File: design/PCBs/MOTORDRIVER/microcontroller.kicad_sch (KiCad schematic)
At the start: 14 parts, among them IC1 ATSAME53J18A-MF

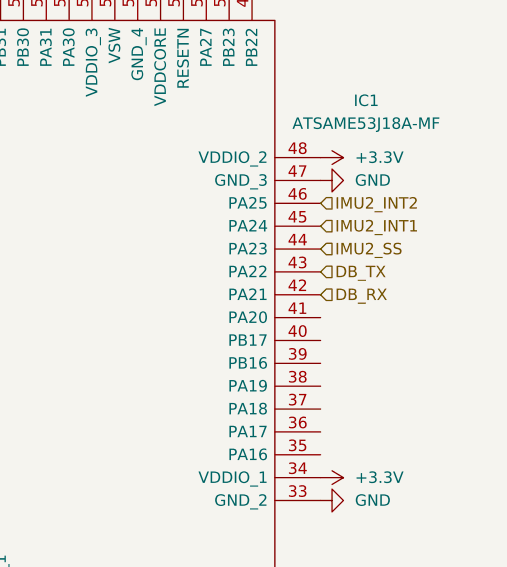
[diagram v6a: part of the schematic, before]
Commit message: added power ic
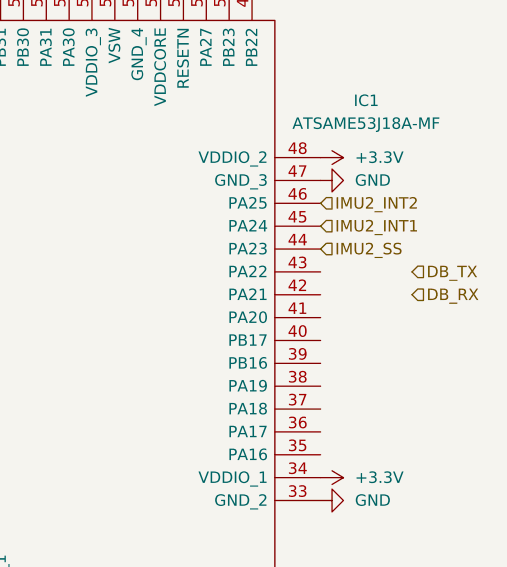
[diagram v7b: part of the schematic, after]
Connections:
- net DB_RX: no longer IC1.42 (PA21)
- net DB_TX: no longer IC1.43 (PA22)
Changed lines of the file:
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@@
 	(hierarchical_label "DB_RX"
 		(shape input)
-		(at 173.99 105.41 0)
+		(at 184.15 105.41 0)
 		(fields_autoplaced yes)
 		(effects
@@
 	(hierarchical_label "DB_TX"
 		(shape input)
-		(at 173.99 102.87 0)
+		(at 184.15 102.87 0)
 		(fields_autoplaced yes)
 		(effects

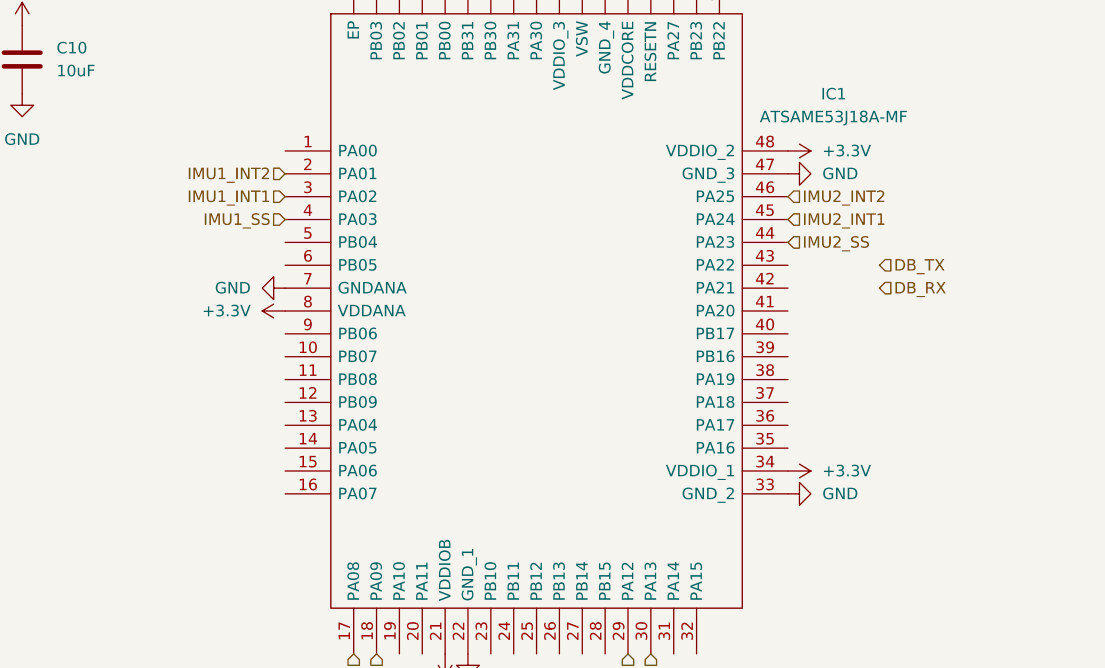
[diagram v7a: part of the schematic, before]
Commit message: Added micro-servo headers Added header for FFC cable IMU PCB
We need to set IMU PCB input to correspond to
the one we have made here.
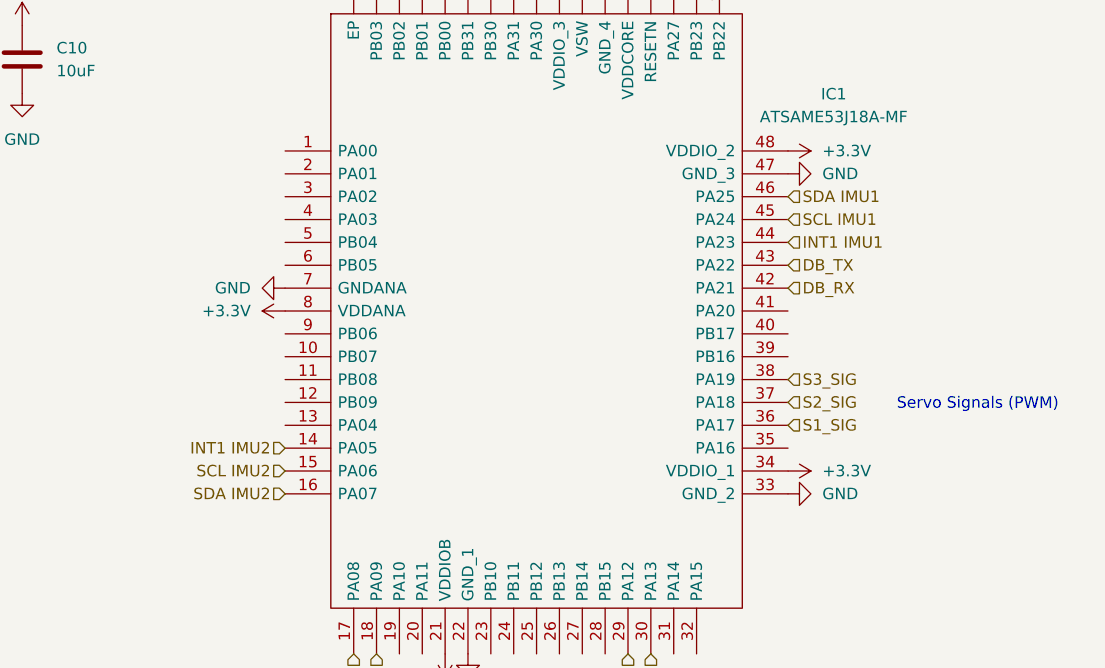
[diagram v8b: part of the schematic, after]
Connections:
- net DB_RX: now also IC1.42 (PA21)
- net DB_TX: now also IC1.43 (PA22)
- net INT1 IMU2: now reaches IC1.14 (PA05)
- net SCL IMU2: now reaches IC1.15 (PA06)
- net SDA IMU2: now reaches IC1.16 (PA07)
- net S1_SIG: now reaches IC1.36 (PA17)
- net S2_SIG: now reaches IC1.37 (PA18)
- net S3_SIG: now reaches IC1.38 (PA19)
- net IMU1_INT1: no longer names the net of IC1.3 (PA02)
- net IMU1_INT2: no longer names the net of IC1.2 (PA01)
- net IMU1_SS: no longer names the net of IC1.4 (PA03)
- net IMU2_INT1 renamed SCL IMU1
- net IMU2_INT2 renamed SDA IMU1
- net IMU2_SS renamed INT1 IMU1
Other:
- note added: "Servo Signals (PWM)"
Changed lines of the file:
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@@
+		)
+	)
+	(text "Servo Signals (PWM)"
+		(exclude_from_sim no)
+		(at 195.072 118.364 0)
+		(effects
+			(font
+				(size 1.27 1.27)
+			)
 		)
 	)
@@
 		)
 	)
+	(hierarchical_label "SDA IMU1"
+		(shape input)
+		(at 173.99 95.25 0)
+		(fields_autoplaced yes)
+		(effects
+			(font
+				(size 1.27 1.27)
+			)
+			(justify left)
+		)
+	)
+	(hierarchical_label "S2_SIG"
+		(shape input)
+		(at 173.99 118.11 0)
+		(fields_autoplaced yes)
+		(effects
+			(font
+				(size 1.27 1.27)
+			)
+			(justify left)
+		)
+	)
 	(hierarchical_label "ERR_LED"
 		(shape input)
@@
 	(hierarchical_label "DB_RX"
 		(shape input)
-		(at 184.15 105.41 0)
+		(at 173.99 105.41 0)
 		(fields_autoplaced yes)
 		(effects
@@
 	(hierarchical_label "DB_TX"
 		(shape input)
-		(at 184.15 102.87 0)
-		(fields_autoplaced yes)
-		(effects
-			(font
-				(size 1.27 1.27)
-			)
-			(justify left)
-		)
-	)
-	(hierarchical_label "IMU2_INT1"
+		(at 173.99 102.87 0)
+		(fields_autoplaced yes)
+		(effects
+			(font
+				(size 1.27 1.27)
+			)
+			(justify left)
+		)
+	)
+	(hierarchical_label "S1_SIG"
+		(shape input)
+		(at 173.99 120.65 0)
+		(fields_autoplaced yes)
+		(effects
+			(font
+				(size 1.27 1.27)
+			)
+			(justify left)
+		)
+	)
+	(hierarchical_label "SDA IMU2"
+		(shape input)
+		(at 118.11 128.27 180)
+		(fields_autoplaced yes)
+		(effects
+			(font
+				(size 1.27 1.27)
+			)
+			(justify right)
+		)
+	)
+	(hierarchical_label "SCL IMU2"
+		(shape input)
+		(at 118.11 125.73 180)
+		(fields_autoplaced yes)
+		(effects
+			(font
+				(size 1.27 1.27)
+			)
+			(justify right)
+		)
+	)
+	(hierarchical_label "S3_SIG"
+		(shape input)
+		(at 173.99 115.57 0)
+		(fields_autoplaced yes)
+		(effects
+			(font
+				(size 1.27 1.27)
+			)
+			(justify left)
+		)
+	)
+	(hierarchical_label "SCL IMU1"
 		(shape input)
 		(at 173.99 97.79 0)
@@
 		)
 	)
+	(hierarchical_label "INT1 IMU2"
+		(shape input)
+		(at 118.11 123.19 180)
+		(fields_autoplaced yes)
+		(effects
+			(font
+				(size 1.27 1.27)
+			)
+			(justify right)
+		)
+	)
 	(hierarchical_label "OLED_SCL"
 		(shape input)
@@
 		)
 	)
-	(hierarchical_label "IMU2_INT2"
-		(shape input)
-		(at 173.99 95.25 0)
-		(fields_autoplaced yes)
-		(effects
-			(font
-				(size 1.27 1.27)
-			)
-			(justify left)
-		)
-	)
 	(hierarchical_label "PROCESS_LED"
 		(shape input)
@@
 		)
 	)
-	(hierarchical_label "IMU2_SS"
+	(hierarchical_label "OLED_SDA"
+		(shape input)
+		(at 128.27 146.05 270)
+		(fields_autoplaced yes)
+		(effects
+			(font
+				(size 1.27 1.27)
+			)
+			(justify right)
+		)
+	)
+	(hierarchical_label "INT1 IMU1"
 		(shape input)
 		(at 173.99 100.33 0)
@@
 		)
 	)
-	(hierarchical_label "IMU1_SS"
-		(shape input)
-		(at 118.11 97.79 180)
-		(fields_autoplaced yes)
-		(effects
-			(font
-				(size 1.27 1.27)
-			)
-			(justify right)
-		)
-	)
-	(hierarchical_label "IMU1_INT1"
-		(shape input)
-		(at 118.11 95.25 180)
-		(fields_autoplaced yes)
-		(effects
-			(font
-				(size 1.27 1.27)
-			)
-			(justify right)
-		)
-	)
-	(hierarchical_label "OLED_SDA"
-		(shape input)
-		(at 128.27 146.05 270)
-		(fields_autoplaced yes)
-		(effects
-			(font
-				(size 1.27 1.27)
-			)
-			(justify right)
-		)
-	)
-	(hierarchical_label "IMU1_INT2"
-		(shape input)
-		(at 118.11 92.71 180)
-		(fields_autoplaced yes)
-		(effects
-			(font
-				(size 1.27 1.27)
-			)
-			(justify right)
-		)
-	)
